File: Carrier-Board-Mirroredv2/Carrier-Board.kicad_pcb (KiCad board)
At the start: 4 copper layers, 92 x 96 mm, 118 parts, among them J1 CONN_3-6318491-6, J10 Conn_02x03_Odd_Even, J2 Conn_01x0, J4 SI-51009-F, J6 Conn_01x03_Male, J7 Conn_01x03_Male, J8 Conn_01x06_Male, J9 Conn_02x04_Odd_Even, SW1 SW_Push, SW2 SW_Push, SW3 SW_Push, U1 MPM3620, U2 MPM3620, m1 MountingHole_2.7mm_M2.5_Pad, m2 MountingHole_2.7mm_M2.5_Pad

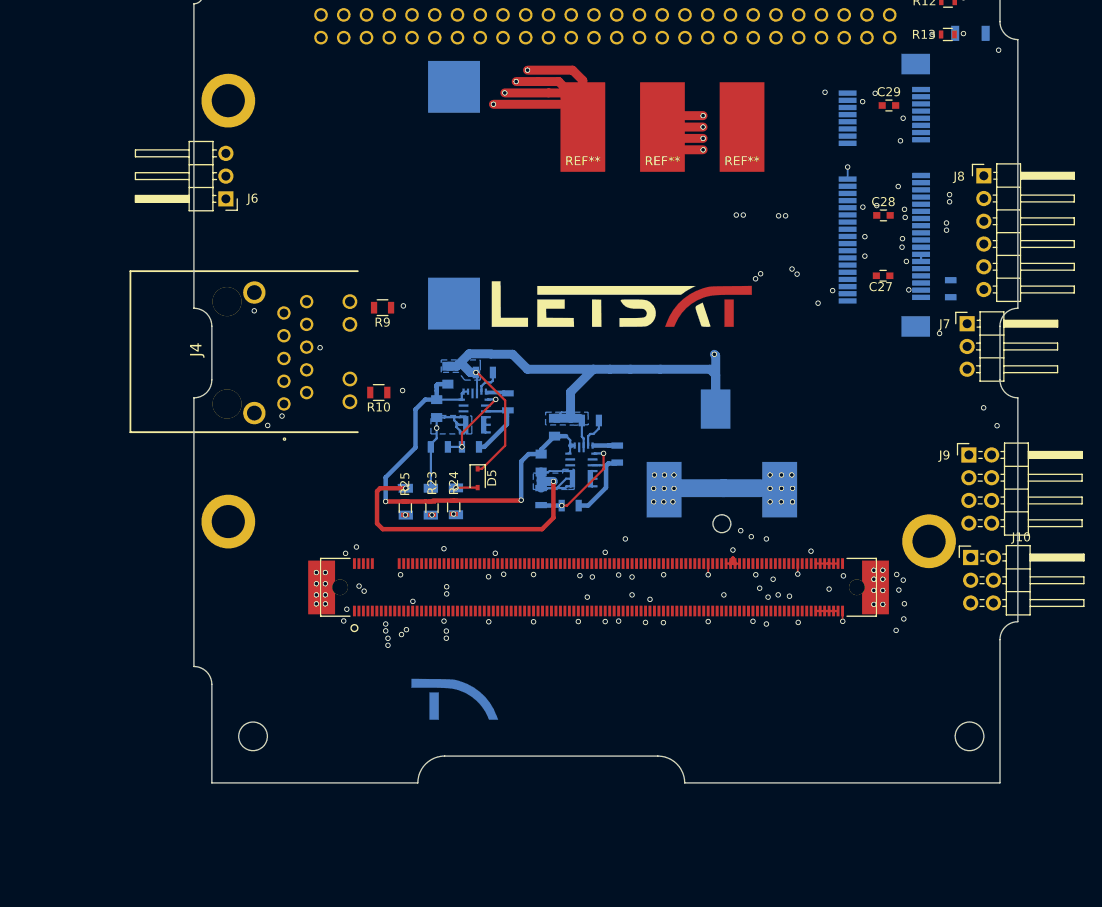
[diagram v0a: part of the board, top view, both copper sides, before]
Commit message: New Mirroredv2 (No Traces yet)
All mounting holes aligned perfectly with original, GPU connector aligned with original, rest of components are matched to ppicture sent to me
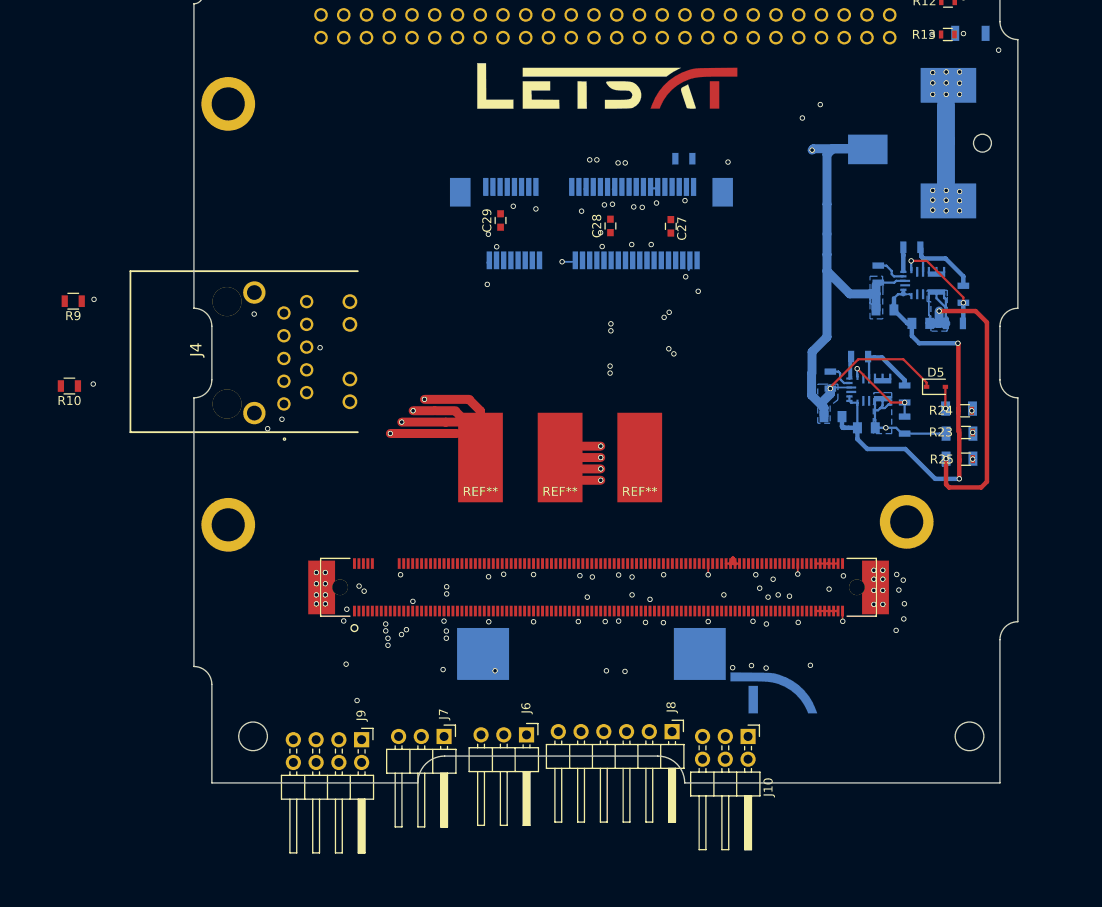
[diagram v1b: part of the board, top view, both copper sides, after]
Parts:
- moved J9 74.9 mm to (181.3, 115.4), turned to 270 degrees
- moved J7 74.4 mm to (190.5, 115.0), turned to 270 degrees
- moved J8 71.2 mm to (215.9, 114.5), turned to 270 degrees
- moved J6 68.6 mm to (199.7, 114.9), turned to 270 degrees
- moved R25 62.8 mm to (248.7, 84.1), turned to 0 degrees
- moved D8 62.0 mm to (248.0, 84.0), turned to 180 degrees
- moved R23 60.2 mm to (248.7, 81.1), turned to 0 degrees
- moved D7 59.5 mm to (248.0, 81.2), turned to 180 degrees
- moved R24 58.1 mm to (248.6, 78.7), turned to 0 degrees
- moved D6 57.1 mm to (248.0, 78.4), turned to 180 degrees
- moved D5 52.2 mm to (245.4, 76.0), turned to 0 degrees
- moved R5 52.0 mm to (241.9, 80.3), turned to 90 degrees
- moved R1 50.0 mm to (247.4, 68.9), turned to 0 degrees
- moved R2 49.8 mm to (248.4, 65.7), turned to 90 degrees
- moved R6 48.8 mm to (241.9, 76.8), turned to 90 degrees
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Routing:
- net GBE0_CTREF(GND): track 496.0 -> 930.5 mm, vias 166 -> 162
- net (no net): track 76.3 -> 493.1 mm, vias 1 -> 4
- net +3.3V: track 458.4 -> 149.1 mm
- net GBE0_MDI2-: track 157.9 -> 81.1 mm, vias 4 -> 3
- net GBE0_LINK100#: track 85.1 -> 10.8 mm
- net GPI1: track 153.1 -> 80.0 mm, vias 2 -> 1
- net mCOM_12V: track 305.0 -> 377.4 mm, vias 6 -> 8
- net GPO3: track 81.5 -> 9.10 mm, vias 2 -> 1
- net GPI3: track 76.9 -> 4.77 mm, vias 2 -> 1
- net GBE0_MDI1+: track 80.1 -> 33.1 mm
- net GBE0_MDI3+: track 127.6 -> 80.7 mm, vias 5 -> 4
- net GBE0_MDI1-: track 81.0 -> 34.8 mm
- net GBE0_MDI3-: track 127.1 -> 81.2 mm
- net GBE0_MDI2+: track 119.3 -> 81.4 mm
- net mCOM_5V_SBY: track 445.6 -> 421.7 mm
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
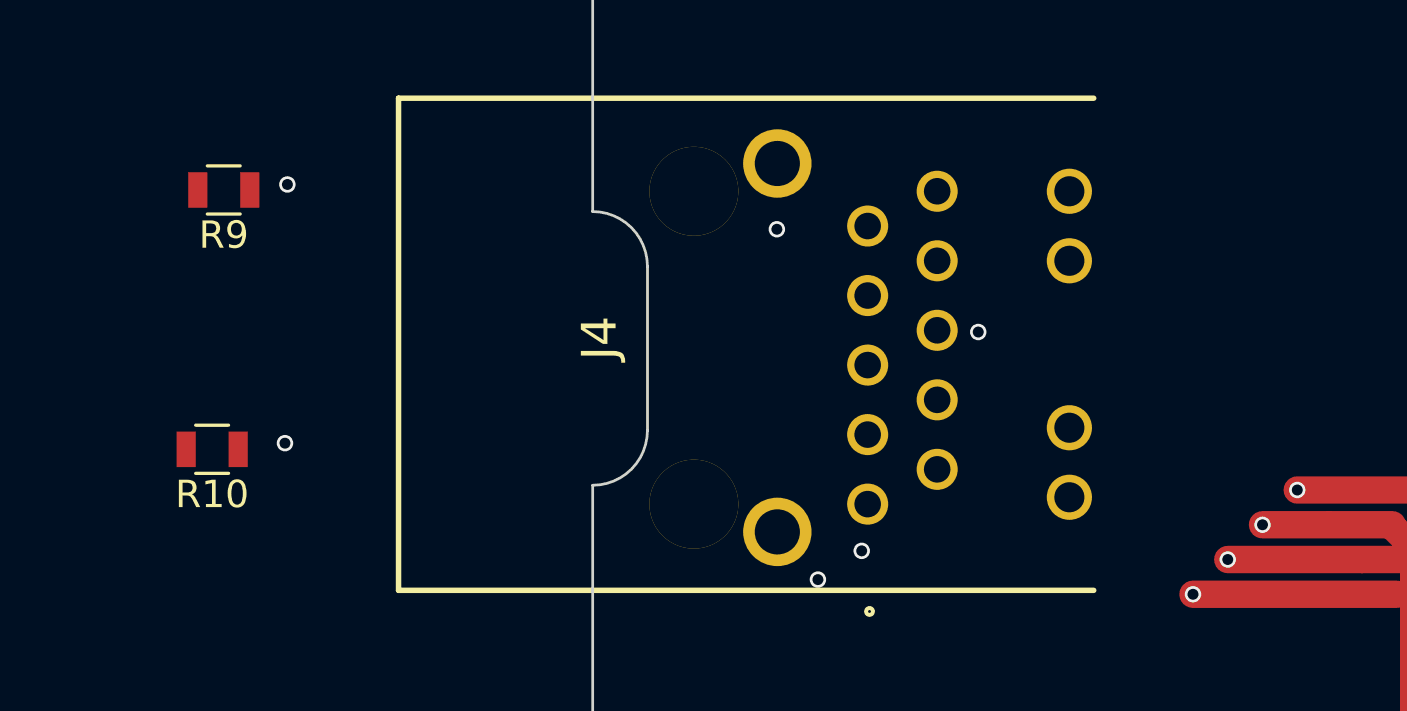
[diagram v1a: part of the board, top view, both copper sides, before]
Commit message: Mirrored Boardv2 new (No Traces)
Mirrored board with all componts and holes aligned as well as GPU connector
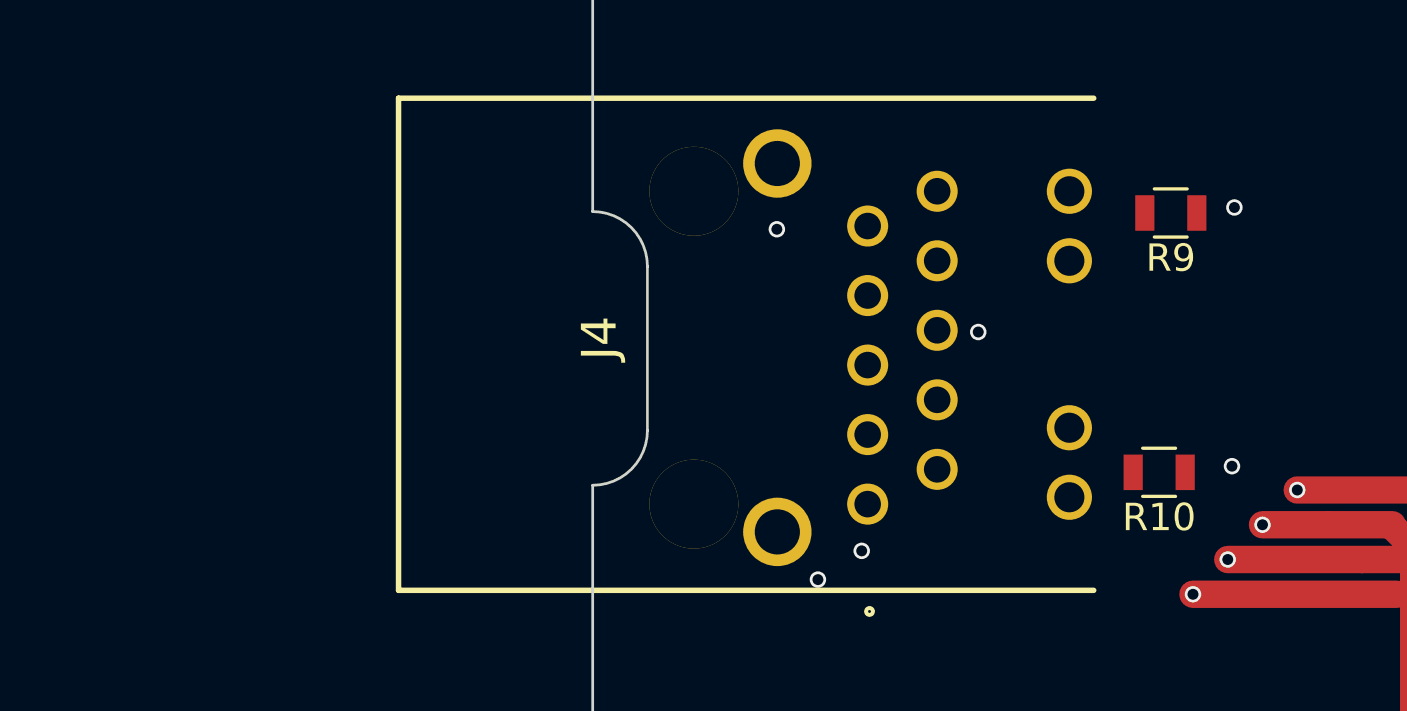
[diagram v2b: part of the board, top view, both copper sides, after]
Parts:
- moved R10 34.6 mm to (183.2, 76.7)
- moved R9 34.6 mm to (183.7, 67.3)

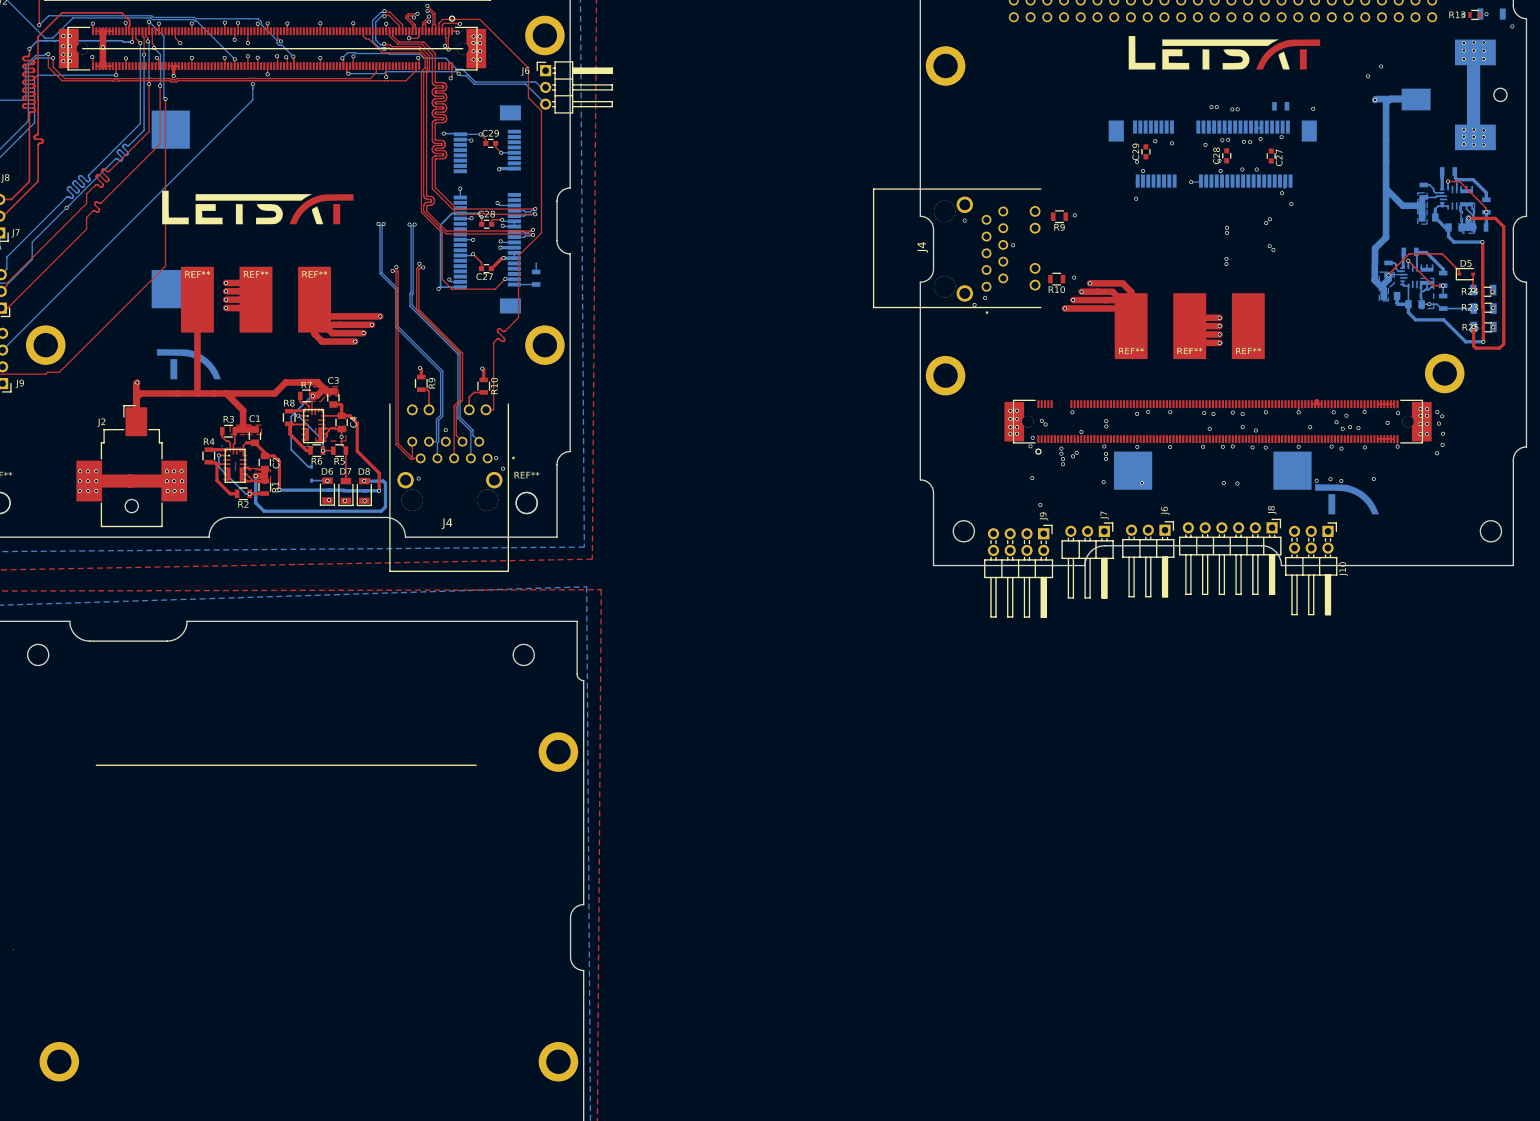
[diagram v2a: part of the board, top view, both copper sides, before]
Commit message: GPU Holes
GPU holes aligned correctly
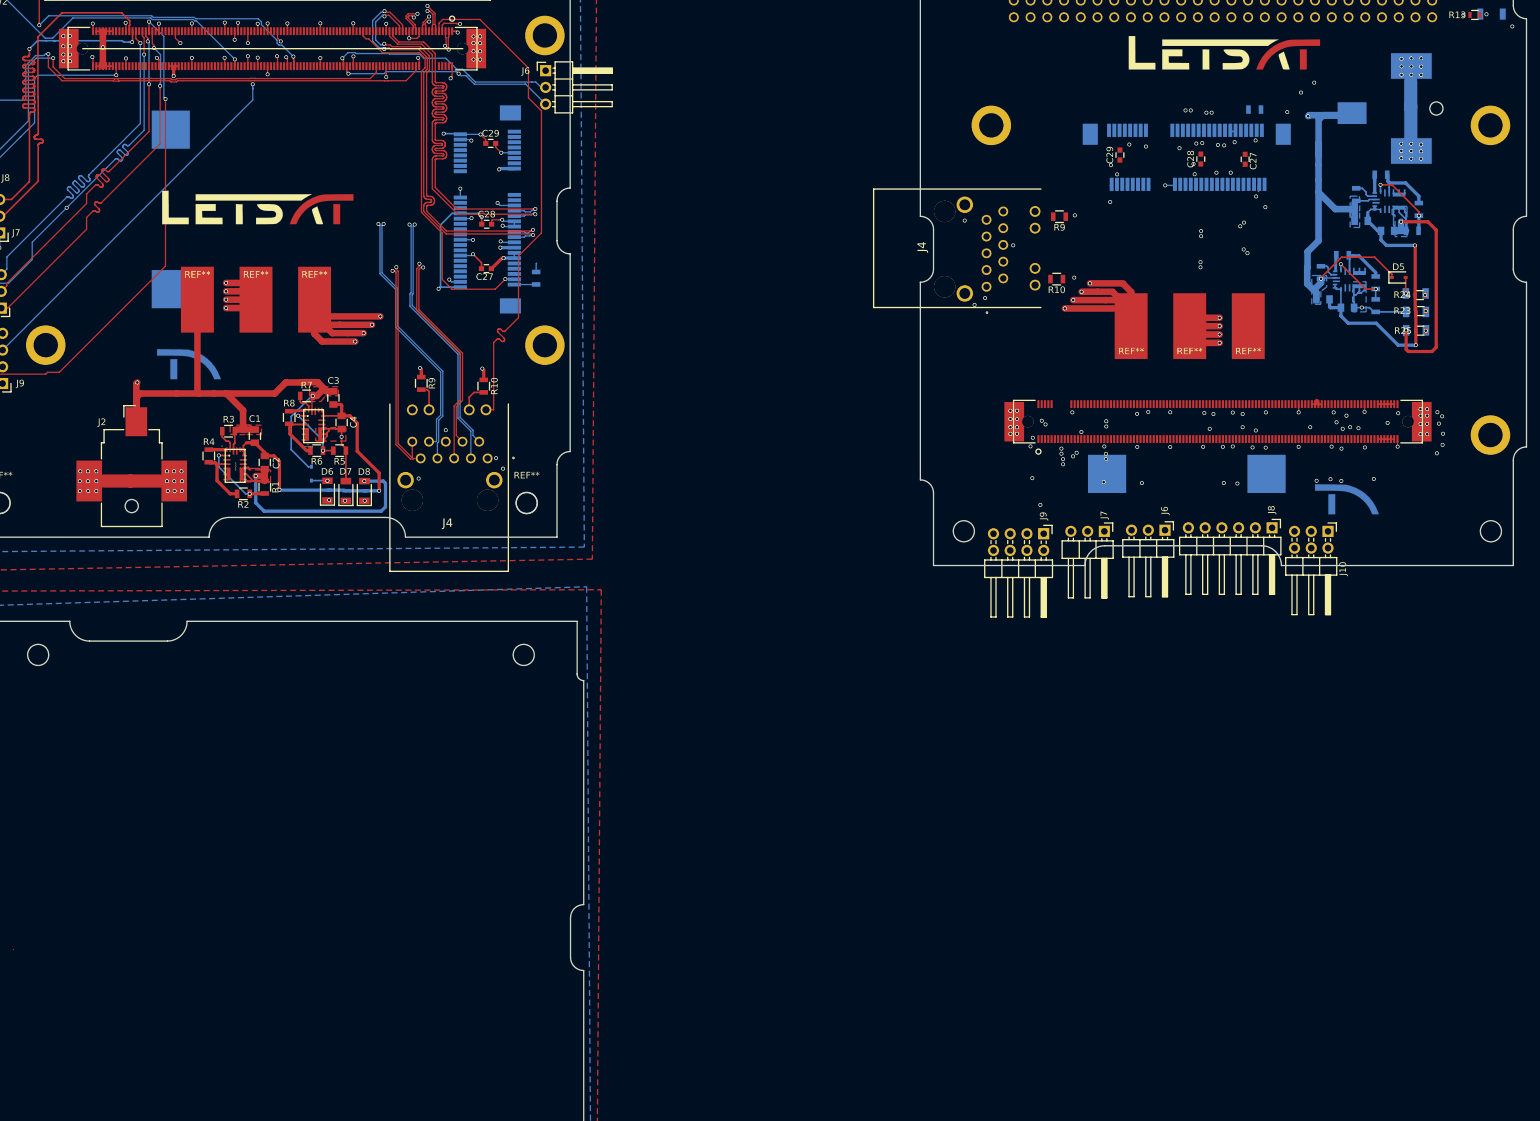
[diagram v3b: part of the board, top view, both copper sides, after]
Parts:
- removed the m1 at (166.4, 44.4)
- removed the m1 at (166.4, 91.4)
- removed the m2 at (242.1, 91.1)
- m1 (x2), m2: moved to B.Cu
- moved m1 200.5 mm to (249.1, 53.4)
- moved m2 200.5 mm to (173.3, 53.4)
- moved m1 149.4 mm to (249.1, 100.4)
- moved C1 10.3 mm to (229.4, 67.9)
- moved C2 10.3 mm to (233.4, 69.4)
- moved D6 10.3 mm to (237.7, 78.9)
- moved R1 10.3 mm to (237.2, 69.4)
- moved R2 10.3 mm to (238.2, 66.2)
- moved R3 10.3 mm to (228.7, 63.9)
- moved R4 10.3 mm to (232.4, 60.9)
- moved R7 10.3 mm to (223.3, 75.8)
- moved U1 10.3 mm to (233.9, 64.9)
- moved U2 10.3 mm to (227.9, 76.8)
- moved C3 10.3 mm to (223.6, 79.8)
- moved C4 10.3 mm to (227.4, 81.1)
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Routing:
- net (no net): track 493.1 -> 494.1 mm, vias 4 -> 7
- net Net-(J1-Pad40): track 0.49 -> 0.00 mm, vias 1 -> 0
- net Net-(J1-Pad38): track 0.49 -> 0.00 mm, vias 1 -> 0
- net GBE0_CTREF(GND): track 930.5 -> 930.4 mm, vias 162 -> 161
